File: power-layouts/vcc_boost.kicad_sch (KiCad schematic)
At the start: 34 parts, among them J1201 RFBT, J1202 RDAC, Q1201 SQJ974EP, U1201 LM5122MHX/NOPB, U1202 DAC53401DSGR

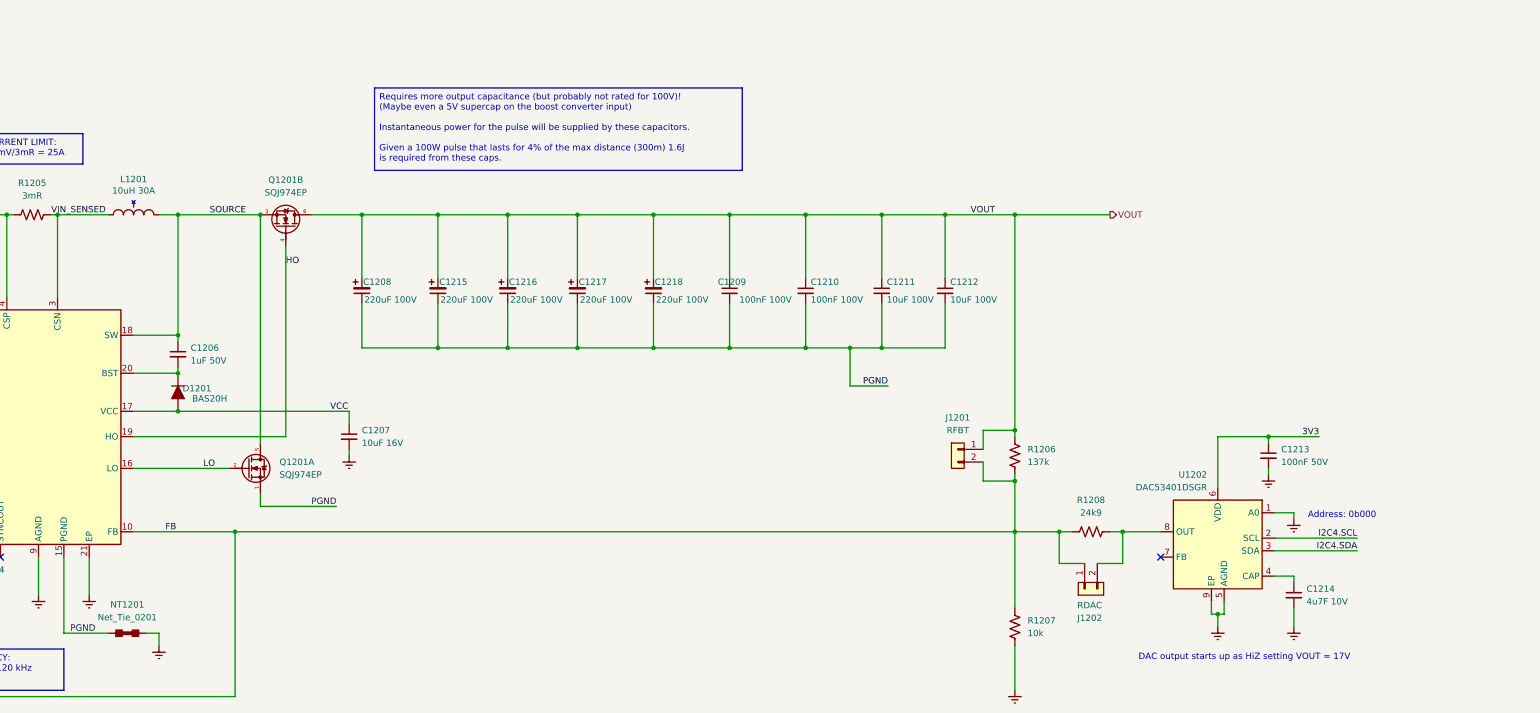
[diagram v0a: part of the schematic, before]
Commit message: Add more VCC boost output capacitance
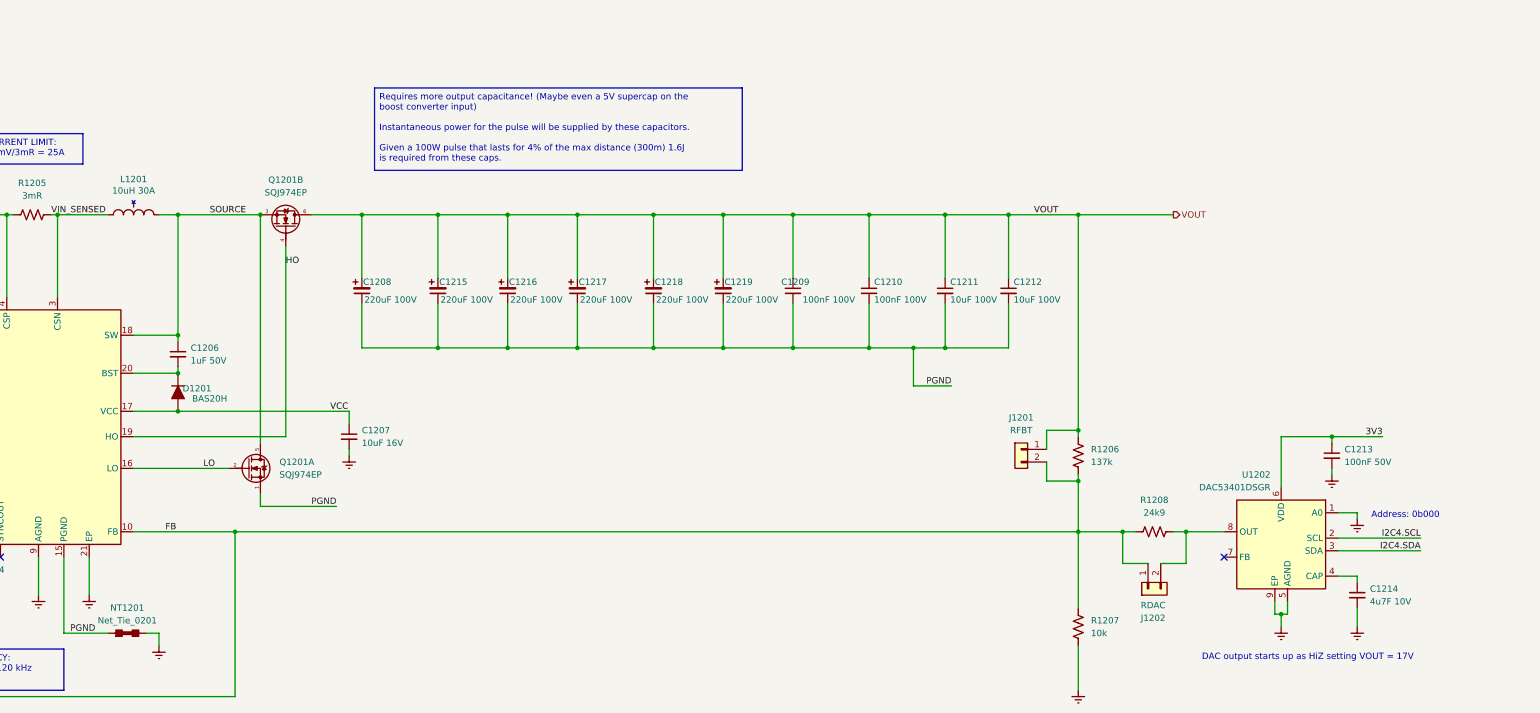
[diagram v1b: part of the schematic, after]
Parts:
- added C1219: 220uF 100V, BR_Passives:C_Elec_12.5x12.5, symbol BR_Capacitors_Electrolytic:C_Alum_220uF_100V_20%_SMD
- NT1201: footprint BR_Virtual_Parts:Net_Tie_0201_1608Metric -> BR_Virtual_Parts:NetTie-2_SMD_Pad_3.88mm_wide; symbol BR_Virtual_Parts:Net_Tie_0201 -> BR_Virtual_Parts:NetTie-2_3.88mm
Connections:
- net PGND: now also C1219.2
- net VOUT: now also C1219.1
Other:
- moved on the sheet: C1209, C1210, C1211, C1212, C1213, C1214, J1201, J1202, R1206, R1207, R1208, U1202
